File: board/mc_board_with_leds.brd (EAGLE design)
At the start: 70.3 x 34.5 mm, 36 parts, among them IC1 TPS61070DDC, IC2 MEGA8-P, Q2 16MHz

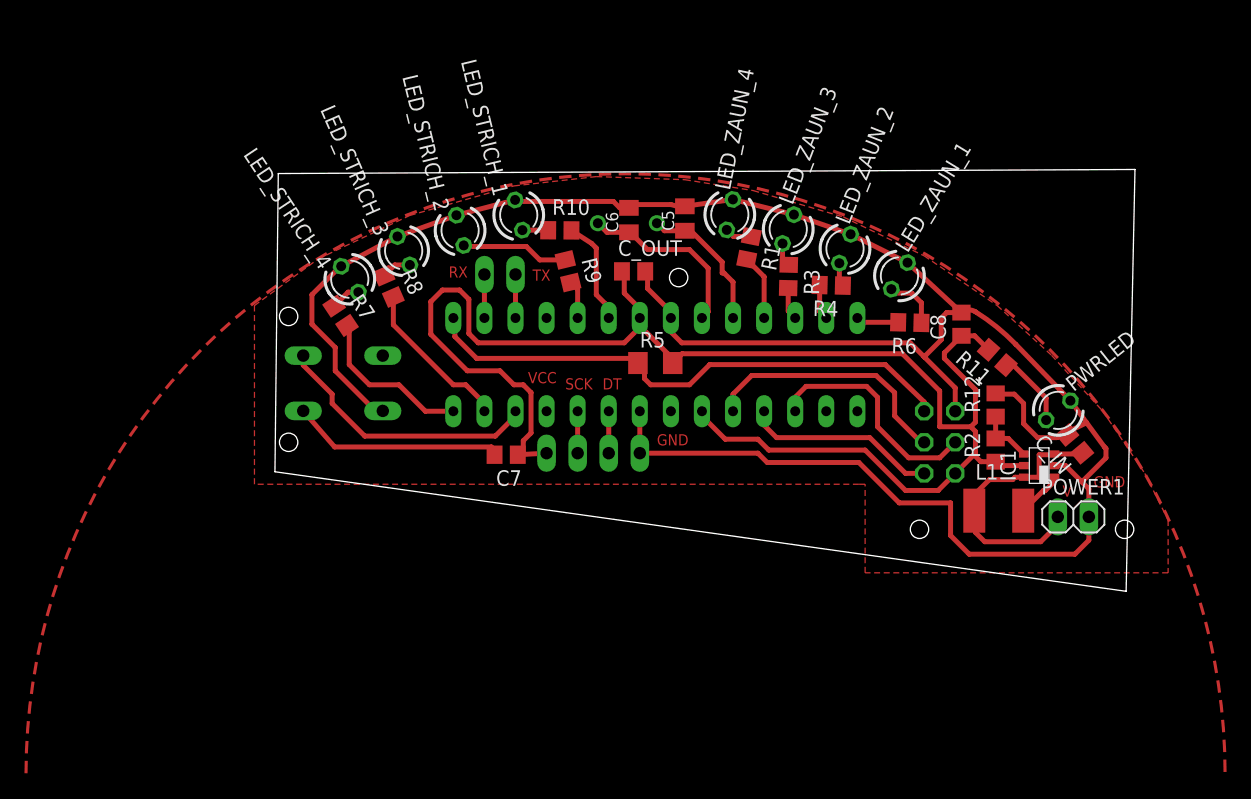
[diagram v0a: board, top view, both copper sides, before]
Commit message: all standard layer now visible again
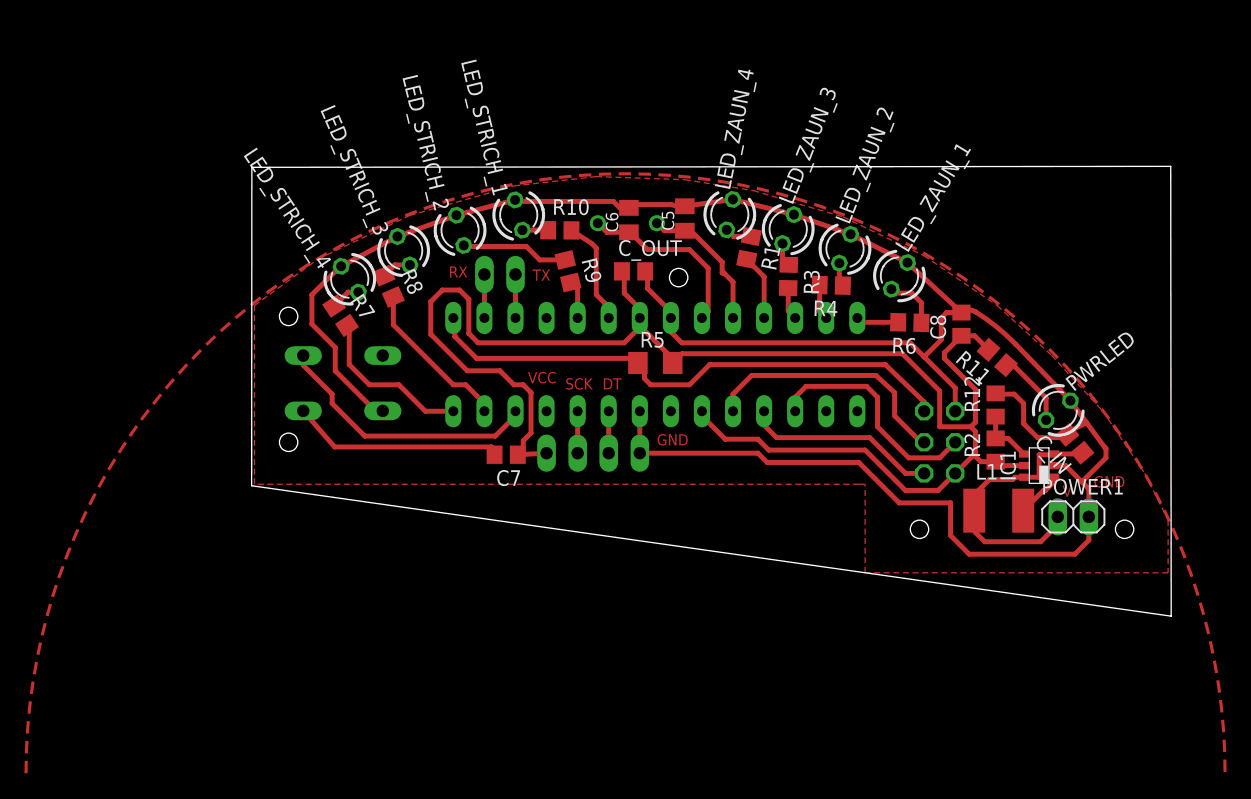
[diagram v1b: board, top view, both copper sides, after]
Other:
- board size 70.3 x 34.5 mm -> 75.2 x 36.8 mm
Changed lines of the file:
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@@
 <layers>
 <layer number="1" name="Top" color="4" fill="1" visible="yes" active="yes"/>
-<layer number="16" name="Bottom" color="1" fill="1" visible="no" active="yes"/>
+<layer number="16" name="Bottom" color="1" fill="1" visible="yes" active="yes"/>
 <layer number="17" name="Pads" color="2" fill="1" visible="yes" active="yes"/>
-<layer number="18" name="Vias" color="2" fill="1" visible="no" active="yes"/>
-<layer number="19" name="Unrouted" color="6" fill="1" visible="no" active="yes"/>
-<layer number="20" name="Dimension" color="15" fill="1" visible="no" active="yes"/>
-<layer number="21" name="tPlace" color="7" fill="1" visible="no" active="yes"/>
-<layer number="22" name="bPlace" color="7" fill="1" visible="no" active="yes"/>
-<layer number="23" name="tOrigins" color="15" fill="1" visible="no" active="yes"/>
-<layer number="24" name="bOrigins" color="15" fill="1" visible="no" active="yes"/>
-<layer number="25" name="tNames" color="7" fill="1" visible="no" active="yes"/>
-<layer number="26" name="bNames" color="7" fill="1" visible="no" active="yes"/>
+<layer number="18" name="Vias" color="2" fill="1" visible="yes" active="yes"/>
+<layer number="19" name="Unrouted" color="6" fill="1" visible="yes" active="yes"/>
+<layer number="20" name="Dimension" color="15" fill="1" visible="yes" active="yes"/>
+<layer number="21" name="tPlace" color="7" fill="1" visible="yes" active="yes"/>
+<layer number="22" name="bPlace" color="7" fill="1" visible="yes" active="yes"/>
+<layer number="23" name="tOrigins" color="15" fill="1" visible="yes" active="yes"/>
+<layer number="24" name="bOrigins" color="15" fill="1" visible="yes" active="yes"/>
+<layer number="25" name="tNames" color="7" fill="1" visible="yes" active="yes"/>
+<layer number="26" name="bNames" color="7" fill="1" visible="yes" active="yes"/>
 <layer number="27" name="tValues" color="7" fill="1" visible="no" active="yes"/>
 <layer number="28" name="bValues" color="7" fill="1" visible="no" active="yes"/>
@@
 <layer number="49" name="Reference" color="7" fill="1" visible="no" active="yes"/>
 <layer number="50" name="dxf" color="7" fill="1" visible="no" active="no"/>
-<layer number="51" name="tDocu" color="7" fill="1" visible="no" active="yes"/>
-<layer number="52" name="bDocu" color="7" fill="1" visible="no" active="yes"/>
+<layer number="51" name="tDocu" color="7" fill="1" visible="yes" active="yes"/>
+<layer number="52" name="bDocu" color="7" fill="1" visible="yes" active="yes"/>
 <layer number="53" name="tGND_GNDA" color="7" fill="9" visible="no" active="no"/>
 <layer number="54" name="bGND_GNDA" color="1" fill="9" visible="no" active="no"/>
@@
 <layer number="154" name="FabDoc2" color="2" fill="1" visible="no" active="no"/>
 <layer number="155" name="FabDoc3" color="7" fill="15" visible="no" active="no"/>
-<layer number="199" name="Contour" color="7" fill="1" visible="yes" active="yes"/>
+<layer number="199" name="Contour" color="7" fill="1" visible="no" active="yes"/>
 <layer number="200" name="200bmp" color="7" fill="1" visible="no" active="yes"/>
 <layer number="201" name="201bmp" color="2" fill="1" visible="no" active="no"/>
@@
 <board>
 <plain>
-<wire x1="20.345471875" y1="24.64364375" x2="20.617596875" y2="49.016115625" width="0" layer="20"/>
-<wire x1="20.617596875" y1="49.016115625" x2="90.63675" y2="49.349575" width="0" layer="20"/>
-<wire x1="90.63675" y1="49.349575" x2="89.912409375" y2="14.87245" width="0" layer="20"/>
-<wire x1="89.912409375" y1="14.87245" x2="20.345471875" y2="24.64364375" width="0" layer="20"/>
+<wire x1="18.440471875" y1="23.50064375" x2="18.458596875" y2="49.524115625" width="0" layer="20"/>
+<wire x1="18.458596875" y1="49.524115625" x2="93.55775" y2="49.603575" width="0" layer="20"/>
+<wire x1="93.55775" y1="49.603575" x2="93.595409375" y2="12.84045" width="0" layer="20"/>
+<wire x1="93.595409375" y1="12.84045" x2="18.440471875" y2="23.50064375" width="0" layer="20"/>
 <text x="34.544" y="40.513" size="0.9144" layer="1" font="vector" ratio="28">RX</text>
 <text x="41.402" y="40.259" size="0.9144" layer="1" font="vector" ratio="28">TX</text>

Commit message: replaced some things on the board
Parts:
- moved C_OUT 27.1 mm to (76.5, 36.8), turned to 90 degrees
- moved C8 27.0 mm to (49.8, 40.8), turned to 0 degrees
- moved R1 1.53 mm to (59.7, 41.5), turned to 268.6 degrees
- moved C6 0.52 mm to (49.4, 45.7)
- moved C5 0.38 mm to (53.8, 45.7)
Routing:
- net PD5/LED_ZAUN_4: track 5.39 -> 3.64 mm
- net N$14: track 14.8 -> 16.3 mm
- net N$4: track 11.7 -> 12.8 mm
- net N$1: track 2.23 -> 3.27 mm
- net GND: track 193.5 -> 194.3 mm

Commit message: added missing values
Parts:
- C_IN: value (none) -> 4.7μF
- C_OUT: value (none) -> 47μF
- L1: value (none) -> 4,7µH
- R_BOT: value (none) -> 330k
- R_TOP: value (none) -> 560k
- renumbered IC1 to MCP1640BT-I, R12 to R_BOT, R2 to R_TOP
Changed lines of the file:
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@@
 <element name="HX1" library="pinhead" package="1X04" value="JP1" x="46.355" y="26.162" rot="MR0"/>
 <element name="UART1" library="pinhead" package="1X02" value="JP2" x="38.735" y="40.767" rot="MR180"/>
-<element name="IC1" library="texas" package="TSOT23-6_DDC" value="TPS61070DDC" x="82.804" y="25.146" rot="R90">
+<element name="MCP1640BT-I" library="texas" package="TSOT23-6_DDC" value="TPS61070DDC" x="82.804" y="25.146" rot="R90">
 <attribute name="MPN" value="TPS61070DDCR" x="82.804" y="25.146" size="1.778" layer="27" rot="R90" display="off"/>
 <attribute name="OC_NEWARK" value="64M3125" x="82.804" y="25.146" size="1.778" layer="27" rot="R90" display="off"/>
@@
 <attribute name="OC_FARNELL" value="1461062" x="82.804" y="25.146" size="1.778" layer="27" rot="R90" display="off"/>
 </element>
-<element name="L1" library="rcl" package="L4532P" value="" x="79.502" y="21.463"/>
-<element name="R2" library="resistor" package="R0805" value="" x="79.248" y="26.416" rot="R90"/>
-<element name="R12" library="resistor" package="R0805" value="" x="79.248" y="30.099" rot="R90"/>
-<element name="C_IN" library="rcl-2" package="C0805" value="" x="85.725" y="26.924" rot="R130"/>
-<element name="C_OUT" library="rcl-2" package="C0805" value="" x="76.454" y="36.83" rot="R90"/>
+<element name="L1" library="rcl" package="L4532P" value="4,7µH" x="79.502" y="21.463"/>
+<element name="R_TOP" library="resistor" package="R0805" value="560k" x="79.248" y="26.416" rot="R90"/>
+<element name="R_BOT" library="resistor" package="R0805" value="330k" x="79.248" y="30.099" rot="R90"/>
+<element name="C_IN" library="rcl-2" package="C0805" value="4.7μF" x="85.725" y="26.924" rot="R130"/>
+<element name="C_OUT" library="rcl-2" package="C0805" value="47μF" x="76.454" y="36.83" rot="R90"/>
 </elements>
 <signals>
@@
 <wire x1="25.273" y1="32.893" x2="25.273" y2="34.798" width="0.4064" layer="1"/>
 <wire x1="25.273" y1="34.798" x2="23.368" y2="36.703" width="0.4064" layer="1"/>
-<contactref element="IC1" pad="2"/>
+<contactref element="MCP1640BT-I" pad="2"/>
 <contactref element="C_IN" pad="2"/>
 <contactref element="C_OUT" pad="2"/>
-<contactref element="R12" pad="2"/>
+<contactref element="R_BOT" pad="2"/>
 <wire x1="28.5496" y1="29.6164" x2="25.273" y2="32.893" width="0.4064" layer="1"/>
 <wire x1="49.403" y1="46.72" x2="49.927" y2="46.482" width="0.4064" layer="1"/>
@@
 <wire x1="35.433" y1="39.497" x2="34.036" y2="39.497" width="0.4064" layer="1"/>
 <wire x1="34.036" y1="39.497" x2="33.081" y2="38.542" width="0.4064" layer="1"/>
-<contactref element="IC1" pad="5"/>
-<contactref element="R2" pad="1"/>
+<contactref element="MCP1640BT-I" pad="5"/>
+<contactref element="R_TOP" pad="1"/>
 <contactref element="C_OUT" pad="1"/>
 <wire x1="33.081" y1="38.542" x2="33.081" y2="35.88" width="0.4064" layer="1"/>
@@
 <signal name="V_IN">
 <contactref element="POWER1" pad="1"/>
-<contactref element="IC1" pad="6"/>
+<contactref element="MCP1640BT-I" pad="6"/>
 <contactref element="C_IN" pad="1"/>
 <contactref element="L1" pad="1"/>
-<contactref element="IC1" pad="3"/>
+<contactref element="MCP1640BT-I" pad="3"/>
 <wire x1="81.554" y1="24.196" x2="82.804" y2="24.196" width="0.4064" layer="1"/>
 <wire x1="82.804" y1="24.196" x2="82.804" y2="26.035" width="0.4064" layer="1"/>
@@
 </signal>
 <signal name="N$5">
-<contactref element="IC1" pad="1"/>
+<contactref element="MCP1640BT-I" pad="1"/>
 <contactref element="L1" pad="2"/>
 <wire x1="84.074" y1="24.176" x2="84.054" y2="24.196" width="0.4064" layer="1"/>
@@
 </signal>
 <signal name="N$6">
-<contactref element="R12" pad="1"/>
-<contactref element="R2" pad="2"/>
-<contactref element="IC1" pad="4"/>
+<contactref element="R_BOT" pad="1"/>
+<contactref element="R_TOP" pad="2"/>
+<contactref element="MCP1640BT-I" pad="4"/>
 <wire x1="79.248" y1="27.366" x2="79.248" y2="29.149" width="0.4064" layer="1"/>
 <wire x1="81.554" y1="26.096" x2="80.284" y2="27.366" width="0.4064" layer="1"/>
